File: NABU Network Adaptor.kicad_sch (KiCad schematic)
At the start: 39 parts, among them J2 PC, J3 RF Module, J5 LEDs, U1 SN74LS164N, U10 UA9638CP, U11 UA9637ATC, U12 SN74LS164N, U13 SN74LS164N, U14 SN74LS04N, U15 SN74LS74AN, U19 LM339N, U2 74LS30, U20 SN74LS164N, U21 SN74LS86N, U22 SN74LS74AN, U23 SN74LS74AN, U24 SN74LS04N, U27 SN74LS00P, U3 74LS27, U31 SC87253P, U4 SN74LS164N, U8 110A332, U9 TRI863PL-02

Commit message: Fix MR on U1 and U4
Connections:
- net at R3.2, U12.9 (~{MR}), U13.9 (~{MR})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: no longer U1.9 (~{MR}), U22.4 (~{S}), U4.9 (~{MR})
- new net: U1.9 (~{MR}), U22.4 (~{S}), U4.9 (~{MR})
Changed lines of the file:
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@@
   (junction (at 381.2027 280.67) (diameter 0) (color 0 0 0 0)
   )
-  (junction (at 403.86 346.1062) (diameter 0) (color 0 0 0 0)
-  )
   (junction (at 331.0509 426.72) (diameter 0) (color 0 0 0 0)
   )
@@
     (stroke (width 0) (type default))
   )
-  (wire (pts (xy 316.87 346.1062) (xy 316.87 361.1196))
-    (stroke (width 0) (type default))
-  )
   (wire (pts (xy 493.504 200.66) (xy 493.504 300.99))
     (stroke (width 0) (type default))
@@
     (stroke (width 0) (type default))
   )
-  (wire (pts (xy 426.72 325.12) (xy 406.7292 325.12))
+  (wire (pts (xy 426.72 325.12) (xy 403.86 325.12))
     (stroke (width 0) (type default))
   )
@@
     (stroke (width 0) (type default))
   )
-  (wire (pts (xy 403.86 346.1062) (xy 406.7292 346.1062))
-    (stroke (width 0) (type default))
-  )
   (wire (pts (xy 426.72 332.74) (xy 422.2051 332.74))
     (stroke (width 0) (type default))
@@
     (stroke (width 0) (type default))
   )
-  (wire (pts (xy 316.87 361.1196) (xy 319.1847 361.1196))
-    (stroke (width 0) (type default))
-  )
   (wire (pts (xy 336.9547 312.42) (xy 338.2247 312.42))
     (stroke (width 0) (type default))
@@
     (stroke (width 0) (type default))
   )
-  (wire (pts (xy 316.87 346.1062) (xy 403.86 346.1062))
-    (stroke (width 0) (type default))
-  )
   (wire (pts (xy 327.66 419.1) (xy 334.01 419.1))
     (stroke (width 0) (type default))
@@
     (stroke (width 0) (type default))
   )
-  (wire (pts (xy 406.7292 325.12) (xy 406.7292 346.1062))
-    (stroke (width 0) (type default))
-  )
   (wire (pts (xy 406.8903 401.32) (xy 406.8903 450.6174))
     (stroke (width 0) (type default))
@@
     (stroke (width 0) (type default))
   )
-  (wire (pts (xy 319.1847 361.1196) (xy 319.1847 364.49))
-    (stroke (width 0) (type default))
-  )
   (wire (pts (xy 300.99 464.82) (xy 290.6107 464.82))
     (stroke (width 0) (type default))
@@
     (stroke (width 0) (type default))
   )
-  (wire (pts (xy 403.86 346.1062) (xy 403.86 420.37))
-    (stroke (width 0) (type default))
-  )
+  (wire (pts (xy 403.86 325.12) (xy 403.86 420.37))
+    (stroke (width 0) (type default))
+  )

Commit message: Filling out untraced pins and some cleanup.
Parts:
- added U29: SN74LS74AN, symbol 74xx:74LS74
- added U5: PAL16R6CN, symbol Connector_Generic:Conn_02x10_Counter_Clockwise
- added U6: 74LS374, symbol 74xx:74LS374
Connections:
- net at U22.11 (C): now also U15.3 (C)
- net at U22.12 (D): now also U15.11 (C), U15.6 (~{Q})
- net at U22.13 (~{R}): now also U15.2 (D), U27.12
- net at U15.13 (~{R}): now also U15.1 (~{R})
- net at U15.9 (Q): now also U14.9, U29.11 (C)
- net at U14.13, U3.4: now also CB1.2, U1.12 (Q6)
- net at U1.8 (CP), U12.8 (CP), U13.8 (CP)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: no longer U23.5 (Q)
- net at U27.5: now also U14.8, U23.5 (Q), U5.1 (Pin_1), U6.11 (Cp)
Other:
- moved on the sheet: C1, C12, C13, C20, CB1, J5, R1, R2, R3, R35, R37, TP1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

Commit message: Plop the rest of the ICs on the schematic
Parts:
- added U16: N8X60N, symbol Connector_Generic:Conn_02x14_Counter_Clockwise
- added U17: MN2114-4, symbol Connector_Generic:Conn_02x09_Counter_Clockwise
- added U18: 2114, symbol Connector_Generic:Conn_02x09_Counter_Clockwise
- added unit 2 of U23
- added unit 3 of U23
- added U25: There is no U25, symbol 74xx:74LS373
- added U26, U28, U32: SN74LS74AN, symbol 74xx:74LS74
- added U30: 74LS02, symbol 74xx:74LS02
- added U33: MM74HCU04N, symbol 74xx:74HC04
- added U7: HD74LS373P, symbol 74xx:74LS373

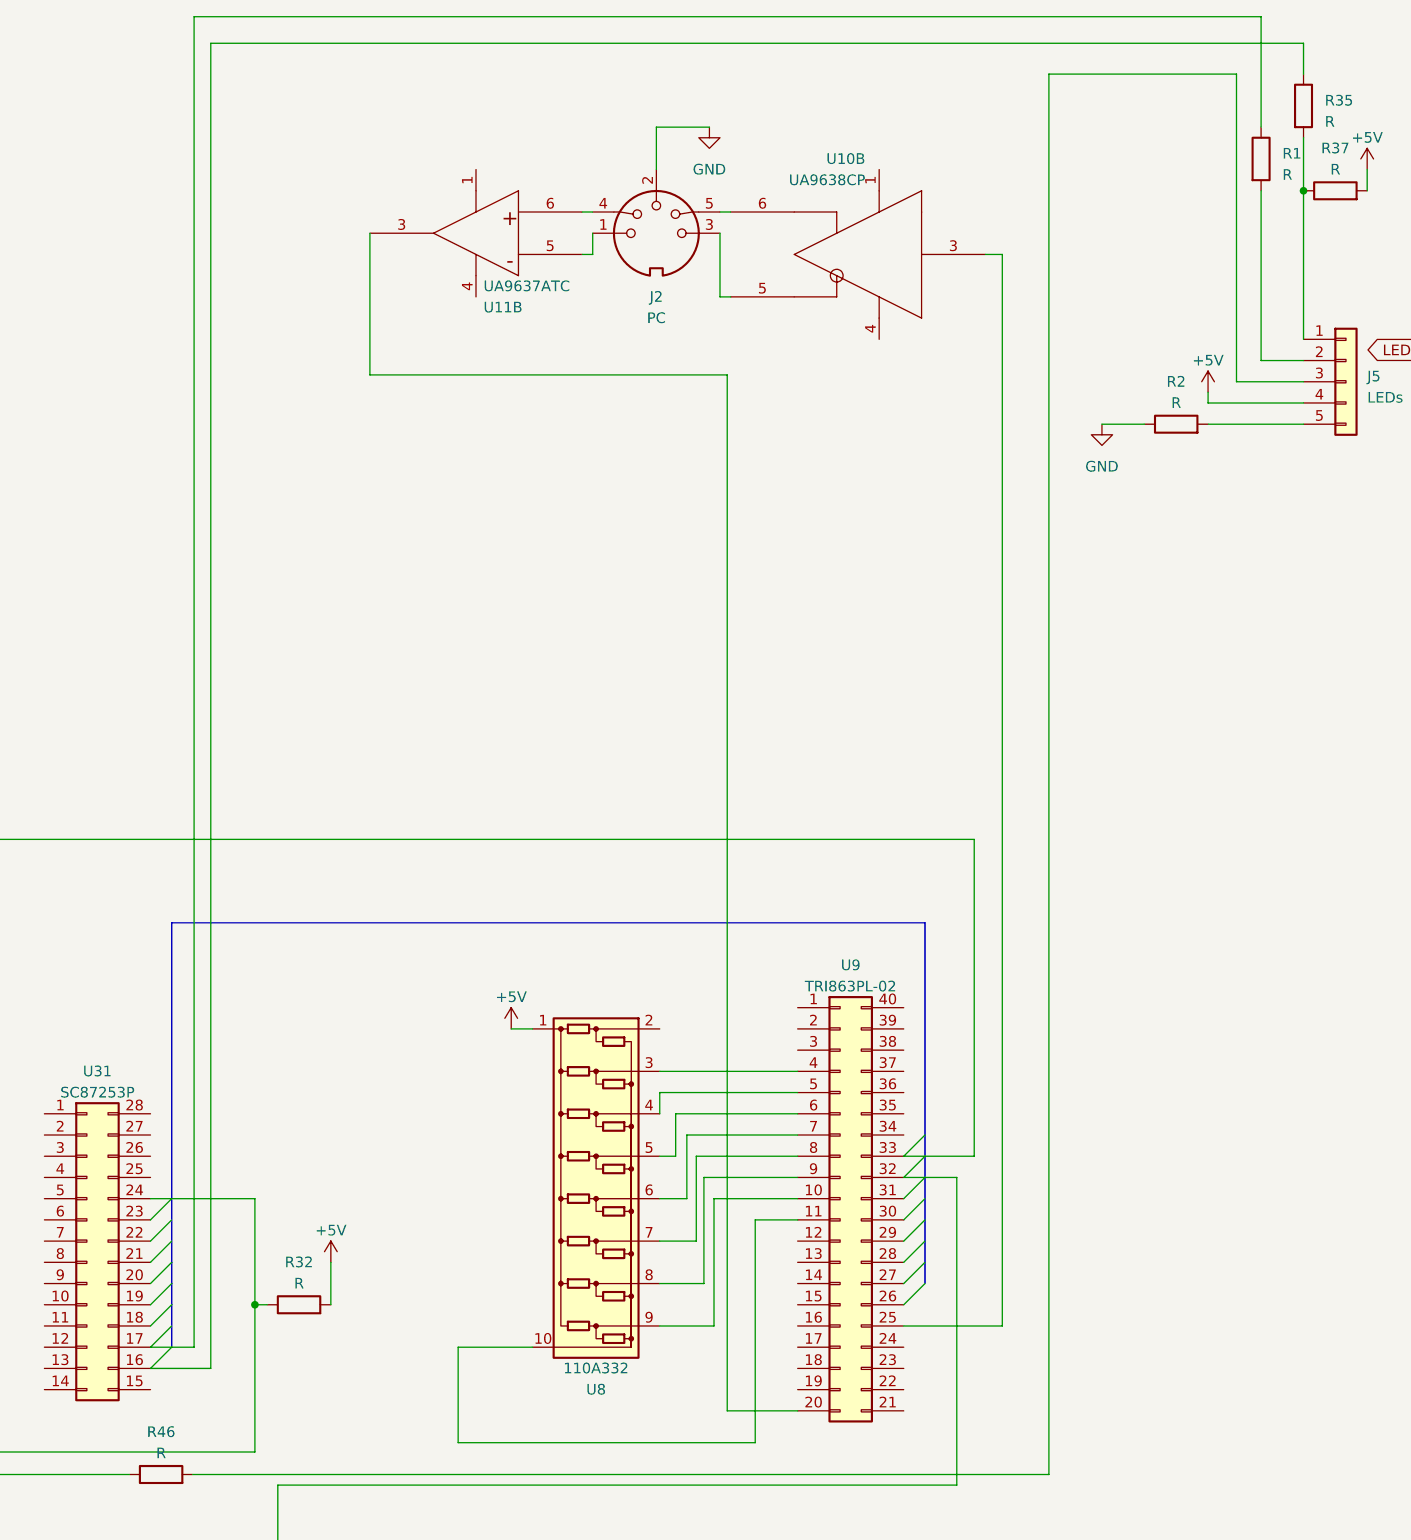
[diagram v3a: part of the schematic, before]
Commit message: Assume U31 is a 6502P2 or P6 and fix LED and UART connections
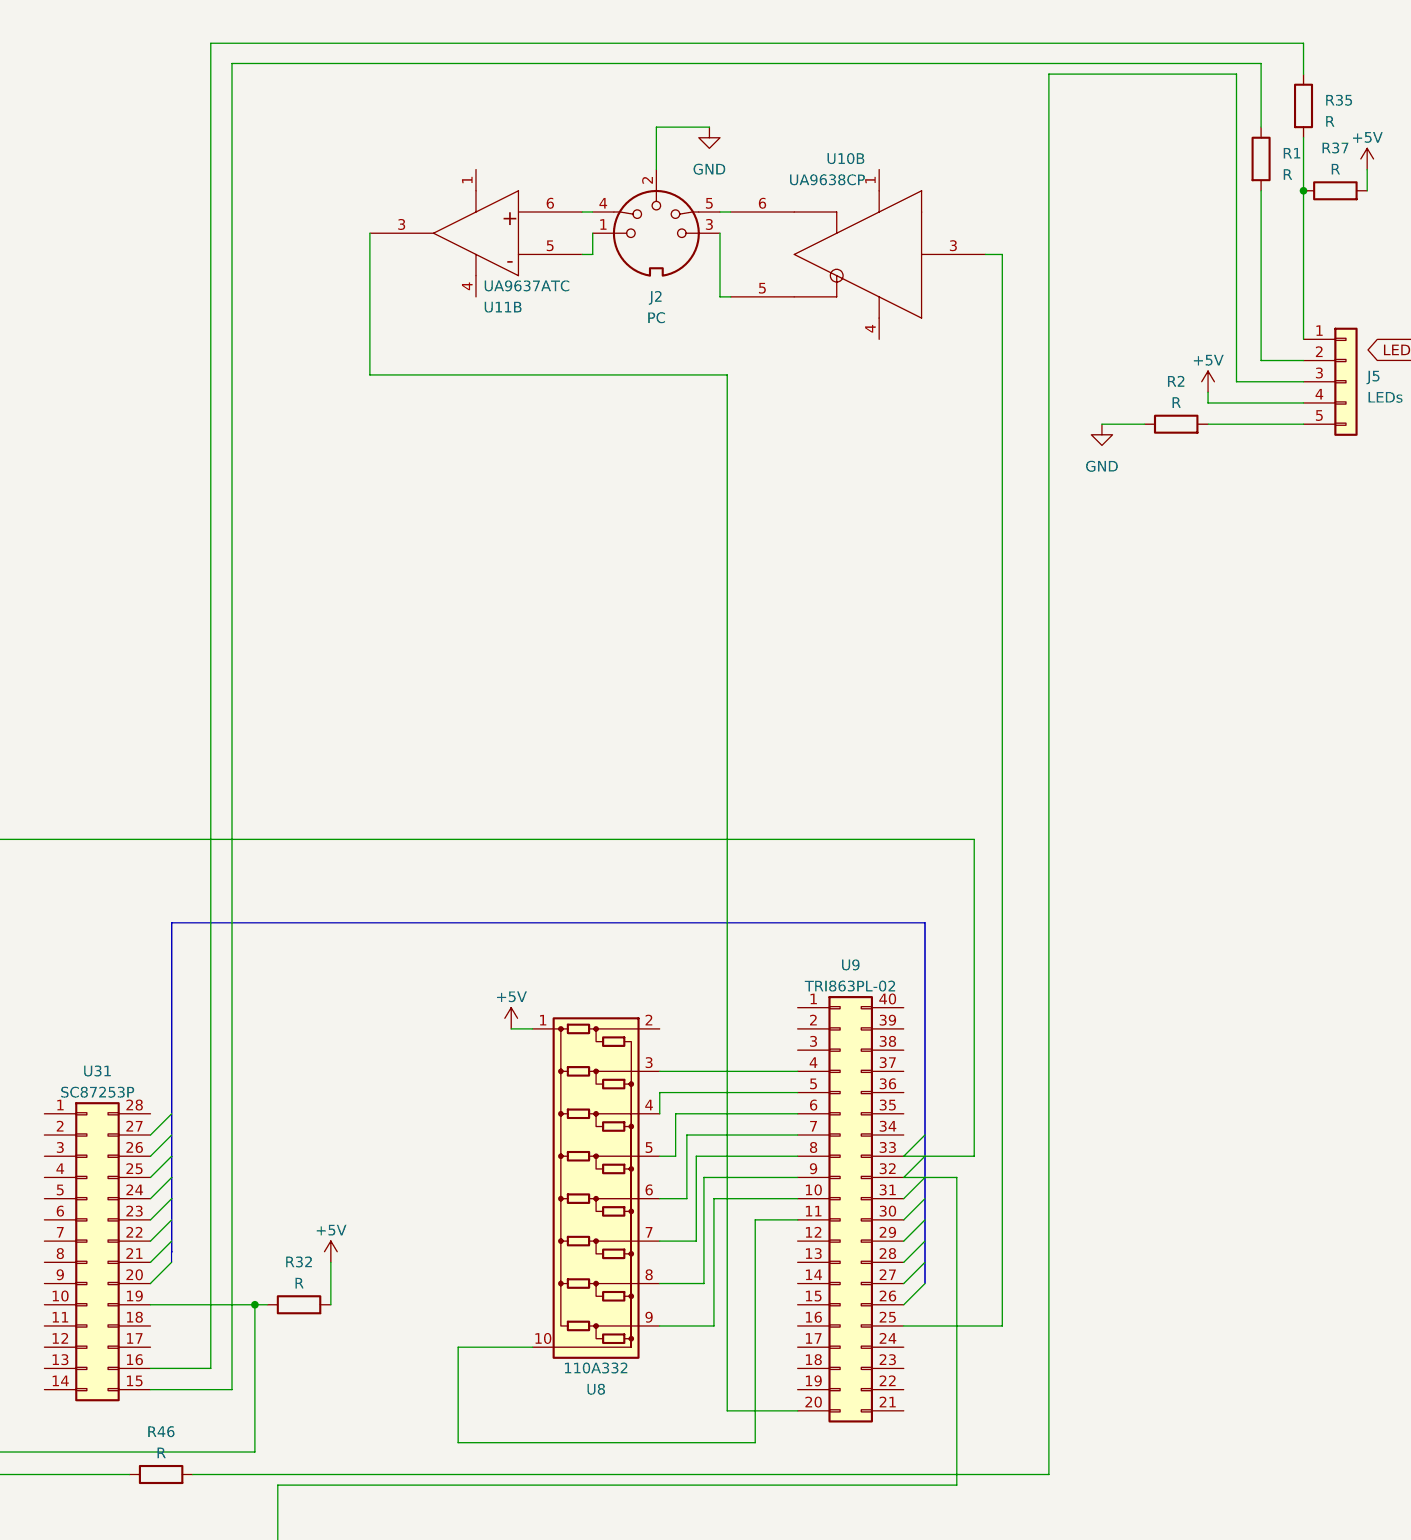
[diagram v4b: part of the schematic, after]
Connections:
- net at R1.1: now also U31.15 (Pin_15); no longer U31.17 (Pin_17)
- net at J3.2 (Pin_2), R32.1: now also U31.19 (Pin_19); no longer U31.24 (Pin_24)
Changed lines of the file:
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@@
     (stroke (width 0) (type default))
   )
-  (bus_entry (at 368.7047 283.21) (size 2.54 -2.54)
+  (bus_entry (at 368.7047 273.05) (size 2.54 -2.54)
     (stroke (width 0) (type default))
   )
@@
     (stroke (width 0) (type default))
   )
+  (bus_entry (at 368.7047 260.35) (size 2.54 -2.54)
+    (stroke (width 0) (type default))
+  )
   (bus_entry (at 458.8747 275.59) (size 2.54 -2.54)
     (stroke (width 0) (type default))
@@
     (stroke (width 0) (type default))
   )
-  (bus_entry (at 368.7047 280.67) (size 2.54 -2.54)
+  (bus_entry (at 368.7047 270.51) (size 2.54 -2.54)
     (stroke (width 0) (type default))
   )
-  (bus_entry (at 368.7047 288.29) (size 2.54 -2.54)
+  (bus_entry (at 368.6881 278.13) (size 2.54 -2.54)
     (stroke (width 0) (type default))
   )
-  (bus_entry (at 368.7047 285.75) (size 2.54 -2.54)
+  (bus_entry (at 368.7047 275.59) (size 2.54 -2.54)
     (stroke (width 0) (type default))
   )
-  (bus_entry (at 368.7047 278.13) (size 2.54 -2.54)
+  (bus_entry (at 368.7047 267.97) (size 2.54 -2.54)
     (stroke (width 0) (type default))
   )
-  (bus_entry (at 368.7047 273.05) (size 2.54 -2.54)
+  (bus_entry (at 368.7047 262.89) (size 2.54 -2.54)
     (stroke (width 0) (type default))
   )
@@
     (stroke (width 0) (type default))
   )
-  (bus_entry (at 368.7047 275.59) (size 2.54 -2.54)
-    (stroke (width 0) (type default))
-  )
-  (bus_entry (at 368.7047 270.51) (size 2.54 -2.54)
+  (bus_entry (at 368.7047 265.43) (size 2.54 -2.54)
     (stroke (width 0) (type default))
   )
@@
     (stroke (width 0) (type default))
   )
+  (wire (pts (xy 368.7047 290.83) (xy 378.46 290.83))
+    (stroke (width 0) (type default))
+  )
   (wire (pts (xy 485.14 358.14) (xy 462.28 358.14))
     (stroke (width 0) (type default))
@@
     (stroke (width 0) (type default))
   )
-  (bus (pts (xy 371.2447 283.21) (xy 371.2447 280.67))
+  (bus (pts (xy 371.2447 273.05) (xy 371.2447 270.51))
     (stroke (width 0) (type default))
   )
@@
     (stroke (width 0) (type default))
   )
-  (wire (pts (xy 371.2447 267.97) (xy 381.2027 267.97))
-    (stroke (width 0) (type default))
-  )
   (wire (pts (xy 375.92 129.6604) (xy 375.92 288.29))
     (stroke (width 0) (type default))
@@
     (stroke (width 0) (type default))
   )
-  (wire (pts (xy 381.2027 280.67) (xy 381.2027 298.2974))
-    (stroke (width 0) (type default))
-  )
   (wire (pts (xy 461.4147 265.43) (xy 458.8747 265.43))
     (stroke (width 0) (type default))
@@
     (stroke (width 0) (type default))
   )
+  (bus (pts (xy 371.2447 265.43) (xy 371.2447 262.89))
+    (stroke (width 0) (type default))
+  )
   (wire (pts (xy 441.0947 297.18) (xy 405.5347 297.18))
     (stroke (width 0) (type default))
@@
     (stroke (width 0) (type default))
   )
+  (wire (pts (xy 501.65 132.08) (xy 501.65 139.7))
+    (stroke (width 0) (type default))
+  )
   (wire (pts (xy 521.97 342.9) (xy 521.97 353.06))
     (stroke (width 0) (type default))
@@
     (stroke (width 0) (type default))
   )
-  (bus (pts (xy 371.2447 285.75) (xy 371.2447 283.21))
+  (bus (pts (xy 371.2281 275.59) (xy 371.2281 274.32))
     (stroke (width 0) (type default))
   )
@@
     (stroke (width 0) (type default))
   )
-  (bus (pts (xy 371.2447 273.05) (xy 371.2447 270.51))
+  (bus (pts (xy 371.2447 262.89) (xy 371.2447 260.35))
     (stroke (width 0) (type default))
   )
@@
     (stroke (width 0) (type default))
   )
-  (wire (pts (xy 371.2447 285.75) (xy 373.9214 285.75))
-    (stroke (width 0) (type default))
-  )
   (wire (pts (xy 470.6721 283.21) (xy 470.6721 154.94))
     (stroke (width 0) (type default))
@@
     (stroke (width 0) (type default))
   )
+  (bus (pts (xy 371.2447 274.32) (xy 371.2447 273.05))
+    (stroke (width 0) (type default))
+  )
   (wire (pts (xy 740.41 407.67) (xy 720.5207 407.67))
     (stroke (width 0) (type default))
@@
     (stroke (width 0) (type default))
   )
-  (wire (pts (xy 373.9214 285.75) (xy 373.9214 126.4807))
+  (wire (pts (xy 378.46 132.08) (xy 378.46 290.83))
     (stroke (width 0) (type default))
   )
@@
     (stroke (width 0) (type default))
   )
+  (wire (pts (xy 378.46 132.08) (xy 501.65 132.08))
+    (stroke (width 0) (type default))
+  )
   (wire (pts (xy 335.28 368.3) (xy 347.98 368.3))
     (stroke (width 0) (type default))
@@
     (stroke (width 0) (type default))
   )
+  (wire (pts (xy 368.7047 288.29) (xy 375.92 288.29))
+    (stroke (width 0) (type default))
+  )
   (wire (pts (xy 335.28 458.47) (xy 476.25 458.47))
     (stroke (width 0) (type default))
@@
     (stroke (width 0) (type default))
   )
-  (bus (pts (xy 371.2447 270.51) (xy 371.2447 267.97))
-    (stroke (width 0) (type default))
-  )
-  (wire (pts (xy 373.9214 126.4807) (xy 501.65 126.4807))
-    (stroke (width 0) (type default))
-  )
   (wire (pts (xy 277.2647 334.01) (xy 277.2647 342.9))
     (stroke (width 0) (type default))
@@
     (stroke (width 0) (type default))
   )
-  (wire (pts (xy 368.7047 288.29) (xy 375.92 288.29))
+  (wire (pts (xy 368.6881 278.13) (xy 368.7047 278.13))
     (stroke (width 0) (type default))
   )
@@
     (stroke (width 0) (type default))
   )
+  (wire (pts (xy 381.2027 280.67) (xy 381.2027 298.2974))
+    (stroke (width 0) (type default))
+  )
   (wire (pts (xy 434.9558 278.13) (xy 429.6647 278.13))
     (stroke (width 0) (type default))
   )
-  (bus (pts (xy 371.2447 267.97) (xy 371.2447 234.95))
+  (bus (pts (xy 371.2447 234.95) (xy 371.2447 257.81))
     (stroke (width 0) (type default))
   )
@@
     (stroke (width 0) (type default))
   )
-  (wire (pts (xy 368.7047 285.75) (xy 371.2447 285.75))
+  (bus (pts (xy 371.2447 257.81) (xy 371.2447 260.35))
     (stroke (width 0) (type default))
   )
@@
     (stroke (width 0) (type default))
   )
-  (wire (pts (xy 501.65 126.4807) (xy 501.65 139.7))
-    (stroke (width 0) (type default))
-  )
   (wire (pts (xy 720.5207 396.24) (xy 699.77 396.24))
     (stroke (width 0) (type default))
@@
     (stroke (width 0) (type default))
   )
-  (bus (pts (xy 371.2447 280.67) (xy 371.2447 278.13))
+  (bus (pts (xy 371.2447 270.51) (xy 371.2447 267.97))
     (stroke (width 0) (type default))
   )
@@
     (stroke (width 0) (type default))
   )
-  (bus (pts (xy 371.2447 278.13) (xy 371.2447 275.59))
-    (stroke (width 0) (type default))
-  )
   (wire (pts (xy 347.98 363.22) (xy 347.98 365.76))
     (stroke (width 0) (type default))
@@
     (stroke (width 0) (type default))
   )
-  (bus (pts (xy 371.2447 275.59) (xy 371.2447 273.05))
+  (bus (pts (xy 371.2447 267.97) (xy 371.2447 265.43))
     (stroke (width 0) (type default))
   )
@@
     (stroke (width 0) (type default))
   )
+  (bus (pts (xy 371.2281 274.32) (xy 371.2447 274.32))
+    (stroke (width 0) (type default))
+  )
   (wire (pts (xy 582.93 379.8089) (xy 582.93 400.05))
     (stroke (width 0) (type default))
@@
     (stroke (width 0) (type default))
   )
-  (wire (pts (xy 368.7047 267.97) (xy 371.2447 267.97))
-    (stroke (width 0) (type default))
-  )
   (wire (pts (xy 355.6 345.44) (xy 358.14 345.44))
     (stroke (width 0) (type default))
@@
     (stroke (width 0) (type default))
   )
-  (wire (pts (xy 381.2027 267.97) (xy 381.2027 280.67))
-    (stroke (width 0) (type default))
-  )
   (wire (pts (xy 652.6296 433.7117) (xy 720.5207 433.7117))
     (stroke (width 0) (type default))
@@
     (stroke (width 0) (type default))
   )
+  (wire (pts (xy 368.7047 280.67) (xy 381.2027 280.67))
+    (stroke (width 0) (type default))
+  )
   (wire (pts (xy 431.8 363.22) (xy 431.8 360.68))
     (stroke (width 0) (type default))
@@
       (effects (font (size 1.27 1.27)) hide)
     )
-    (property "Datasheet" "~" (at 361.0847 273.05 0)
+    (property "Datasheet" "Datasheets/6805P_Oct84.pdf" (at 361.0847 273.05 0)
       (effects (font (size 1.27 1.27)) hide)
     )

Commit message: Fix CPU and UART connections and clean up some more
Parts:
- removed U25: There is no U25, symbol 74xx:74LS373
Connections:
- net DATA7: now reaches U10.2 (IN), U9.33 (Pin_33)
- net DATA7: now also U31.27 (Pin_27)
- net DATA6: now reaches U11.8 (IN+), U9.32 (Pin_32)
- net DATA6: now also U31.26 (Pin_26)
- net DATA0: now reaches U9.26 (Pin_26)
- net DATA0: now also U31.20 (Pin_20)
- net DATA1: now reaches U9.27 (Pin_27)
- net DATA1: now also U31.21 (Pin_21)
- net DATA2: now reaches U9.28 (Pin_28)
- net DATA2: now also U31.22 (Pin_22)
- net DATA3: now reaches U9.29 (Pin_29)
- net DATA3: now also U31.23 (Pin_23)
- net DATA4: now reaches U9.30 (Pin_30)
- net DATA4: now also U31.24 (Pin_24)
- net DATA5: now reaches U9.31 (Pin_31)
- net DATA5: now also U31.25 (Pin_25)
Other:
- moved on the sheet: J2, J5, R1, R2, R32, R35, R37, R43, U10A, U10B, U11B, U14G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

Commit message: Some fixes and cleanups
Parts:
- added TP3: TestPoint, symbol Connector:TestPoint
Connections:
- net at U22.9 (Q): now also U15.2 (D), U27.10
- net at U27.2: now also U23.8 (~{Q}), TP3.1
- net at U17.10 (Pin_10): now also U18.10 (Pin_10), U27.8
- net at U16.7 (Pin_7): now also U23.12 (D), U23.13 (~{R})
- net at U23.10 (~{S}): now also U23.6 (~{Q}), U23.9 (Q)
- net at U23.11 (C): now also U27.9
- now unconnected: U22.13 (~{R}), U27.12
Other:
- moved on the sheet: C1, C12, C13, CB1, TP1, TP2, U1, U10A, U11A, U12, U13, U14A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
